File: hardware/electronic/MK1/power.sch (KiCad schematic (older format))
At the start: 6 parts

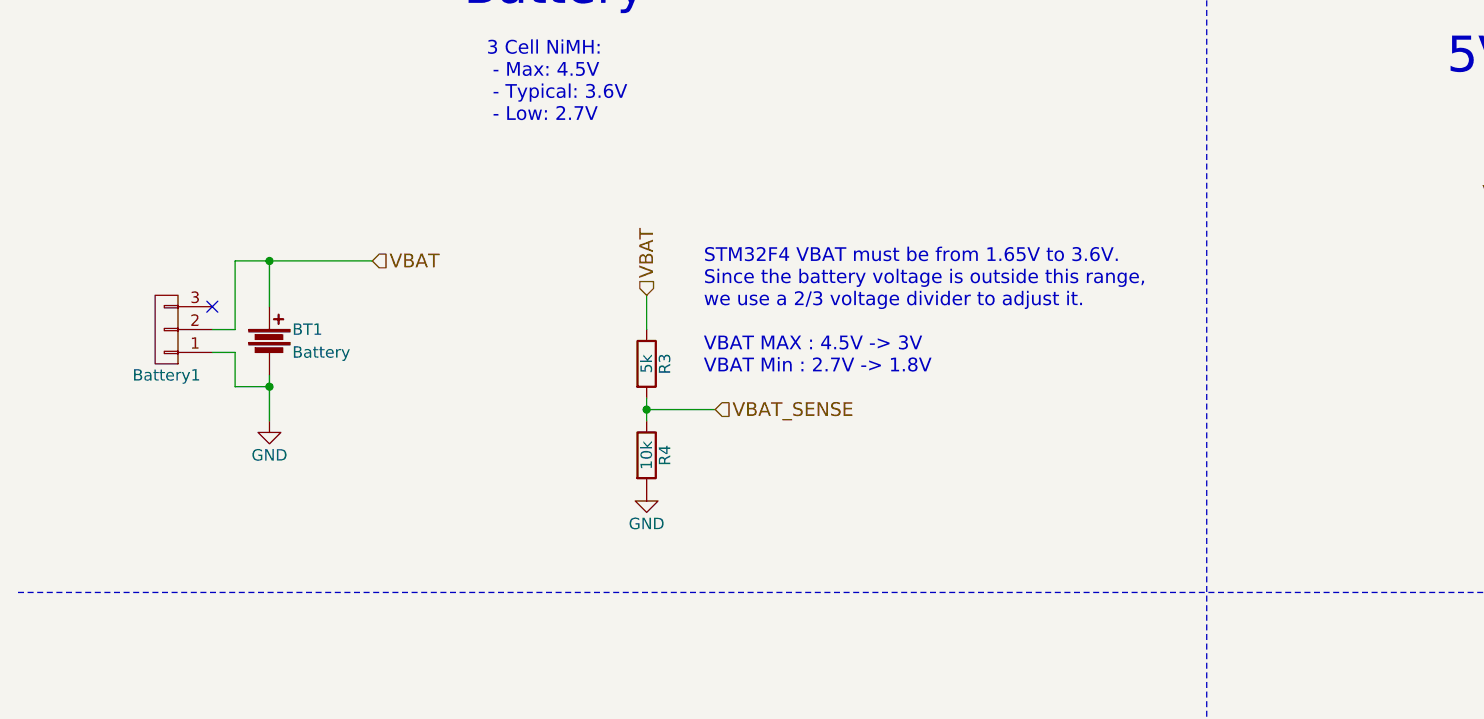
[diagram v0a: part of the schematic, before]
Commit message: HW: Silkscreen and schematic cleanup
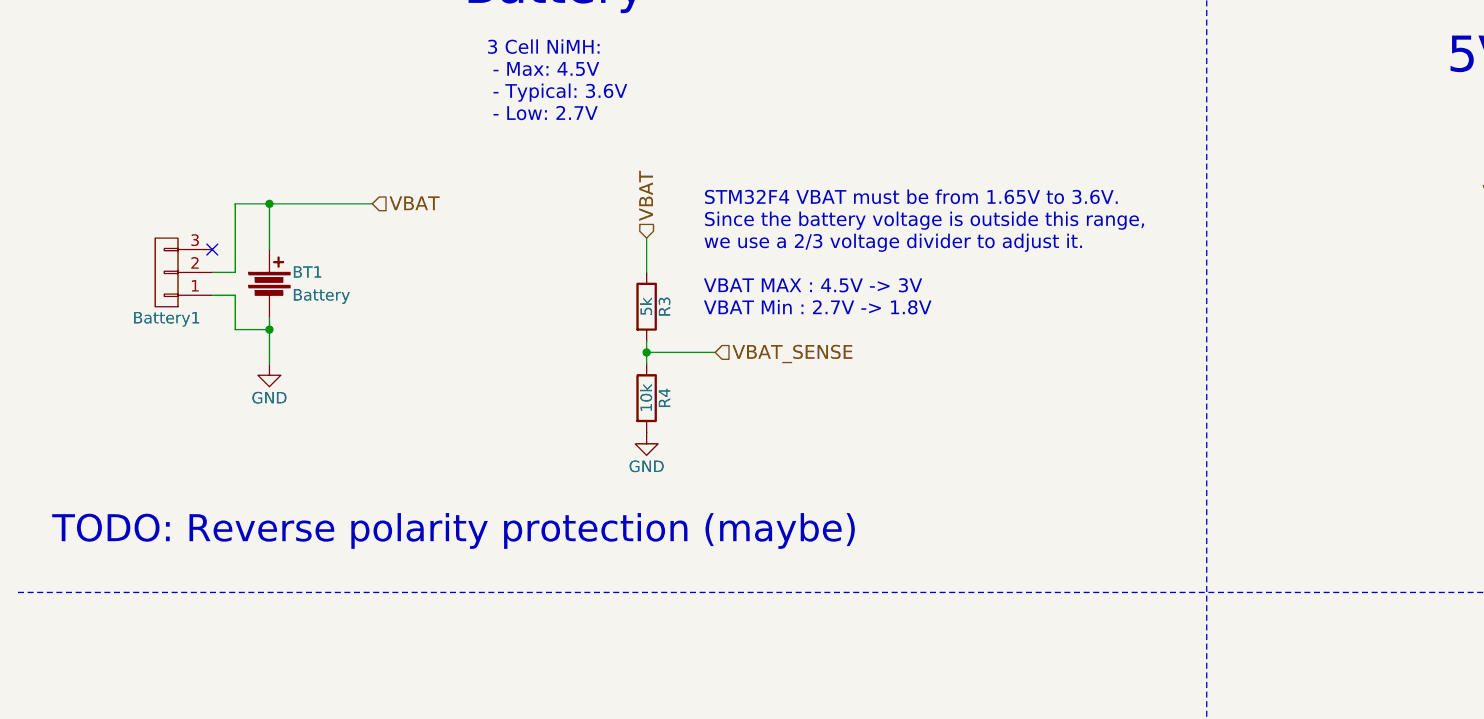
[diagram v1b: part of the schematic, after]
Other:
- note added: "TODO: Reverse polarity protection (maybe)"
- moved on the sheet: BT1, Battery1, R3, R4
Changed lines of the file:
@@
 L Battery BT1
 U 1 1 5885FA38
-P 1650 2250
-F 0 "BT1" H 1750 2300 50  0000 L CNN
-F 1 "Battery" H 1750 2200 50  0000 L CNN
-F 2 "" V 1650 2290 50  0001 C CNN
-F 3 "" V 1650 2290 50  0000 C CNN
-	1    1650 2250
+P 1650 2000
+F 0 "BT1" H 1750 2050 50  0000 L CNN
+F 1 "Battery" H 1750 1950 50  0000 L CNN
+F 2 "" V 1650 2040 50  0001 C CNN
+F 3 "" V 1650 2040 50  0000 C CNN
+	1    1650 2000
 	1    0    0    -1
 $EndComp
@@
 L GND #PWR014
 U 1 1 5885FB0A
-P 1650 2600
-F 0 "#PWR014" H 1650 2350 50  0001 C CNN
-F 1 "GND" H 1650 2450 50  0000 C CNN
-F 2 "" H 1650 2600 50  0000 C CNN
-F 3 "" H 1650 2600 50  0000 C CNN
-	1    1650 2600
+P 1650 2350
+F 0 "#PWR014" H 1650 2100 50  0001 C CNN
+F 1 "GND" H 1650 2200 50  0000 C CNN
+F 2 "" H 1650 2350 50  0000 C CNN
+F 3 "" H 1650 2350 50  0000 C CNN
+	1    1650 2350
 	1    0    0    -1
 $EndComp
@@
 L R R3
 U 1 1 5885FCA2
-P 3300 2350
-F 0 "R3" V 3380 2350 50  0000 C CNN
-F 1 "5k" V 3300 2350 50  0000 C CNN
-F 2 "Resistors_SMD:R_0805" V 3230 2350 50  0001 C CNN
-F 3 "" H 3300 2350 50  0000 C CNN
-	1    3300 2350
+P 3300 2100
+F 0 "R3" V 3380 2100 50  0000 C CNN
+F 1 "5k" V 3300 2100 50  0000 C CNN
+F 2 "Resistors_SMD:R_0805" V 3230 2100 50  0001 C CNN
+F 3 "" H 3300 2100 50  0000 C CNN
+	1    3300 2100
 	1    0    0    -1
 $EndComp
@@
 L R R4
 U 1 1 5885FCD9
-P 3300 2750
-F 0 "R4" V 3380 2750 50  0000 C CNN
-F 1 "10k" V 3300 2750 50  0000 C CNN
-F 2 "Resistors_SMD:R_0805" V 3230 2750 50  0001 C CNN
-F 3 "" H 3300 2750 50  0000 C CNN
-	1    3300 2750
-	1    0    0    -1
-$EndComp
-Wire Wire Line
-	3300 2500 3300 2600
-Wire Wire Line
-	3300 2550 3600 2550
-Connection ~ 3300 2550
+P 3300 2500
+F 0 "R4" V 3380 2500 50  0000 C CNN
+F 1 "10k" V 3300 2500 50  0000 C CNN
+F 2 "Resistors_SMD:R_0805" V 3230 2500 50  0001 C CNN
+F 3 "" H 3300 2500 50  0000 C CNN
+	1    3300 2500
+	1    0    0    -1
+$EndComp
+Wire Wire Line
+	3300 2250 3300 2350
+Wire Wire Line
+	3300 2300 3600 2300
+Connection ~ 3300 2300
 $Comp
 L GND #PWR015
 U 1 1 5885FD97
-P 3300 2900
-F 0 "#PWR015" H 3300 2650 50  0001 C CNN
-F 1 "GND" H 3300 2750 50  0000 C CNN
-F 2 "" H 3300 2900 50  0000 C CNN
-F 3 "" H 3300 2900 50  0000 C CNN
-	1    3300 2900
-	1    0    0    -1
-$EndComp
-Text Notes 3550 2400 0    60   ~ 0
+P 3300 2650
+F 0 "#PWR015" H 3300 2400 50  0001 C CNN
+F 1 "GND" H 3300 2500 50  0000 C CNN
+F 2 "" H 3300 2650 50  0000 C CNN
+F 3 "" H 3300 2650 50  0000 C CNN
+	1    3300 2650
+	1    0    0    -1
+$EndComp
+Text Notes 3550 2150 0    60   ~ 0
 STM32F4 VBAT must be from 1.65V to 3.6V.\nSince the battery voltage is outside this range,\nwe use a 2/3 voltage divider to adjust it.\n\nVBAT MAX : 4.5V -> 3V\nVBAT Min : 2.7V -> 1.8V
-Text HLabel 3600 2550 2    60   Input ~ 0
+Text HLabel 3600 2300 2    60   Input ~ 0
 VBAT_SENSE
 Wire Wire Line
-	3300 2200 3300 2050
-Text HLabel 2100 1900 2    60   Input ~ 0
-VBAT
-Text HLabel 3300 2050 1    60   Input ~ 0
+	3300 1950 3300 1800
+Text HLabel 2100 1650 2    60   Input ~ 0
+VBAT
+Text HLabel 3300 1800 1    60   Input ~ 0
 VBAT
 Text Notes 2500 800  0    157  ~ 0
@@
 	5750 6550 6950 6550
 Wire Wire Line
-	1650 2400 1650 2600
-Wire Wire Line
-	1500 1900 2100 1900
+	1650 2150 1650 2350
+Wire Wire Line
+	1500 1650 2100 1650
 $Comp
 L CONN_01X03 Battery1
 U 1 1 588B953B
-P 1200 2200
-F 0 "Battery1" H 1200 2400 50  0000 C CNN
-F 1 "CONN_01X03" V 1300 2200 50  0001 C CNN
-F 2 "Pin_Headers:Pin_Header_Straight_1x03" H 1200 2200 50  0001 C CNN
-F 3 "" H 1200 2200 50  0000 C CNN
-	1    1200 2200
+P 1200 1950
+F 0 "Battery1" H 1200 2150 50  0000 C CNN
+F 1 "CONN_01X03" V 1300 1950 50  0001 C CNN
+F 2 "Pin_Headers:Pin_Header_Straight_1x03" H 1200 1950 50  0001 C CNN
+F 3 "" H 1200 1950 50  0000 C CNN
+	1    1200 1950
 	-1   0    0    1
 $EndComp
 Wire Wire Line
-	1500 2200 1400 2200
-Wire Wire Line
-	1500 1900 1500 2200
-Wire Wire Line
-	1650 2100 1650 1900
-Connection ~ 1650 1900
-Wire Wire Line
-	1400 2300 1500 2300
-Wire Wire Line
-	1500 2300 1500 2450
-Wire Wire Line
-	1500 2450 1650 2450
-Connection ~ 1650 2450
-NoConn ~ 1400 2100
+	1500 1950 1400 1950
+Wire Wire Line
+	1500 1650 1500 1950
+Wire Wire Line
+	1650 1850 1650 1650
+Connection ~ 1650 1650
+Wire Wire Line
+	1400 2050 1500 2050
+Wire Wire Line
+	1500 2050 1500 2200
+Wire Wire Line
+	1500 2200 1650 2200
+Connection ~ 1650 2200
+NoConn ~ 1400 1850
+Text Notes 700  3150 0    118  ~ 0
+TODO: Reverse polarity protection (maybe)
 $EndSCHEMATC

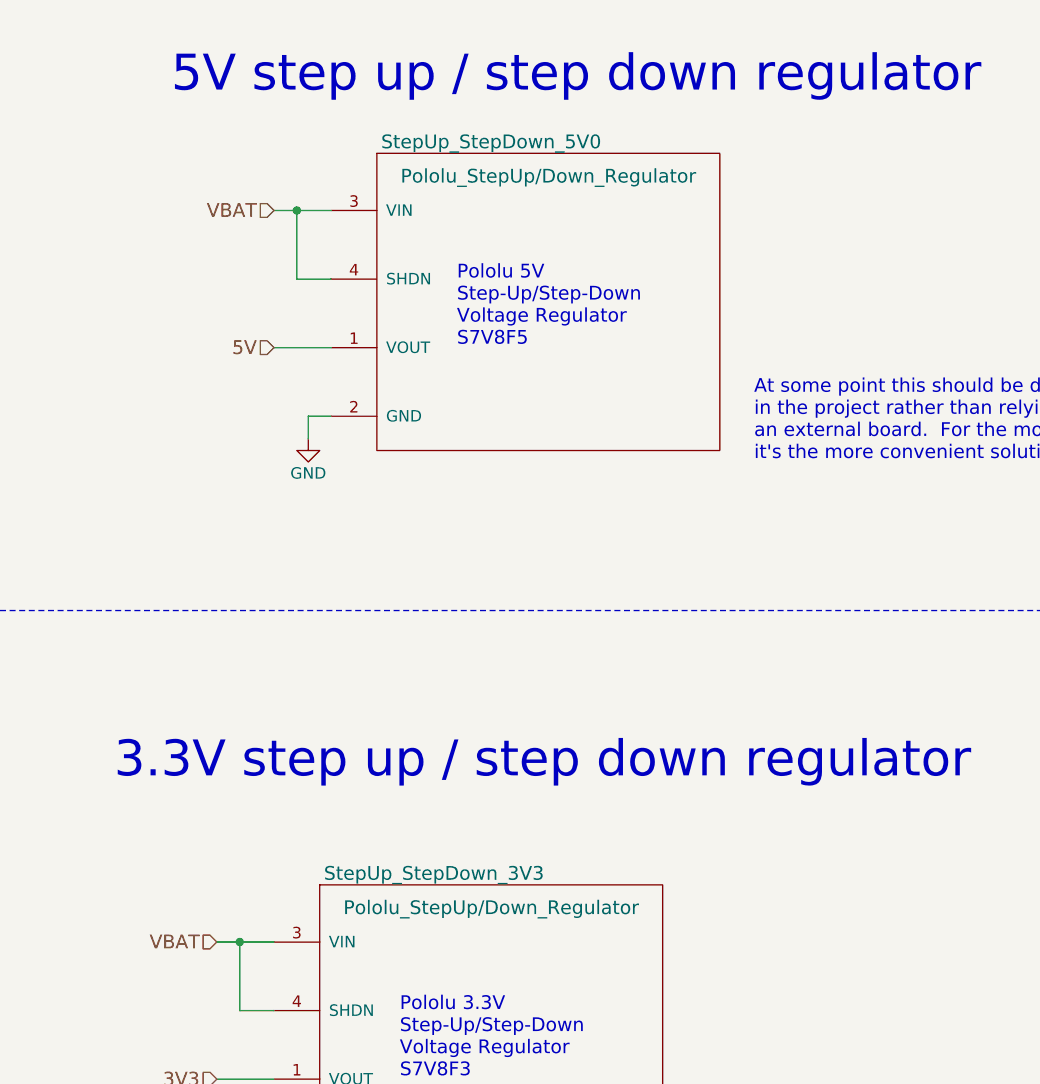
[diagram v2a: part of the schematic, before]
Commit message: HW: Add missing component values
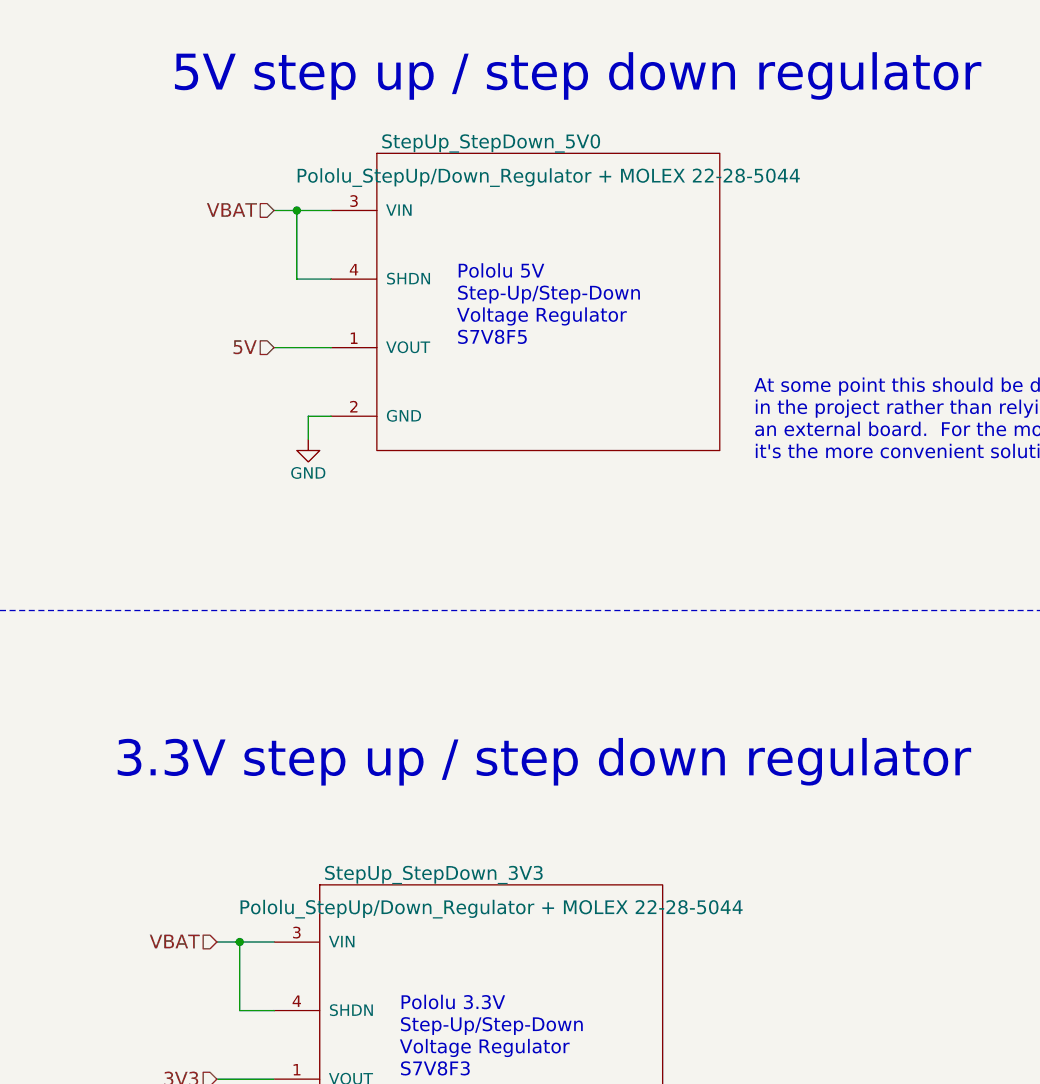
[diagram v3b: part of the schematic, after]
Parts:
- Battery1: value CONN_01X03 -> MOLEX 22-28-4033
- StepUp_StepDown_3V3, StepUp_StepDown_5V0: value Pololu_StepUp/Down_Regulator -> Pololu_StepUp/Down_Regulator + MOLEX 22-28-5044
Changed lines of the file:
@@
 P 7700 1350
 F 0 "StepUp_StepDown_5V0" H 8200 1400 60  0000 C CNN
-F 1 "Pololu_StepUp/Down_Regulator" H 8450 1250 60  0000 C CNN
+F 1 "Pololu_StepUp/Down_Regulator + MOLEX 22-28-5044" H 8450 1250 60  0000 C CNN
 F 2 "OPAVES_Footprints:Pololu_StepUp_StepDown_Regulator" H 7700 1350 60  0001 C CNN
 F 3 "" H 7700 1350 60  0001 C CNN
@@
 P 7450 4550
 F 0 "StepUp_StepDown_3V3" H 7950 4600 60  0000 C CNN
-F 1 "Pololu_StepUp/Down_Regulator" H 8200 4450 60  0000 C CNN
+F 1 "Pololu_StepUp/Down_Regulator + MOLEX 22-28-5044" H 8200 4450 60  0000 C CNN
 F 2 "OPAVES_Footprints:Pololu_StepUp_StepDown_Regulator" H 7450 4550 60  0001 C CNN
 F 3 "" H 7450 4550 60  0001 C CNN
@@
 P 1200 1950
 F 0 "Battery1" H 1200 2150 50  0000 C CNN
-F 1 "CONN_01X03" V 1300 1950 50  0001 C CNN
+F 1 "MOLEX 22-28-4033" V 1300 1950 50  0001 C CNN
 F 2 "Pin_Headers:Pin_Header_Straight_1x03" H 1200 1950 50  0001 C CNN
 F 3 "" H 1200 1950 50  0000 C CNN
